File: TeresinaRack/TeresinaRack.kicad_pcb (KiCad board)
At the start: 8 copper layers, 68 x 40 mm, 198 parts, among them J3 USB_Micro-B, J4 SWD, J5 PATCH_SM_EDGE, Q1 MMBT3904, Q2 MMBT3904, SW1 RESET, SW2 BOOT, U1 STM32H750IBK6, U12 TL074, U13 MCP6004, U14 MCP6004, U15 MCP6004, U16 LM4040DBZ-10, U2 IS25LP064A, U3 AS4C16M32MSA-6BIN, U4 PCM3060, U6 TPS62170DSGR, U7 LD1117S50, U8 USBLC6-2SC6, Y1 16MHz

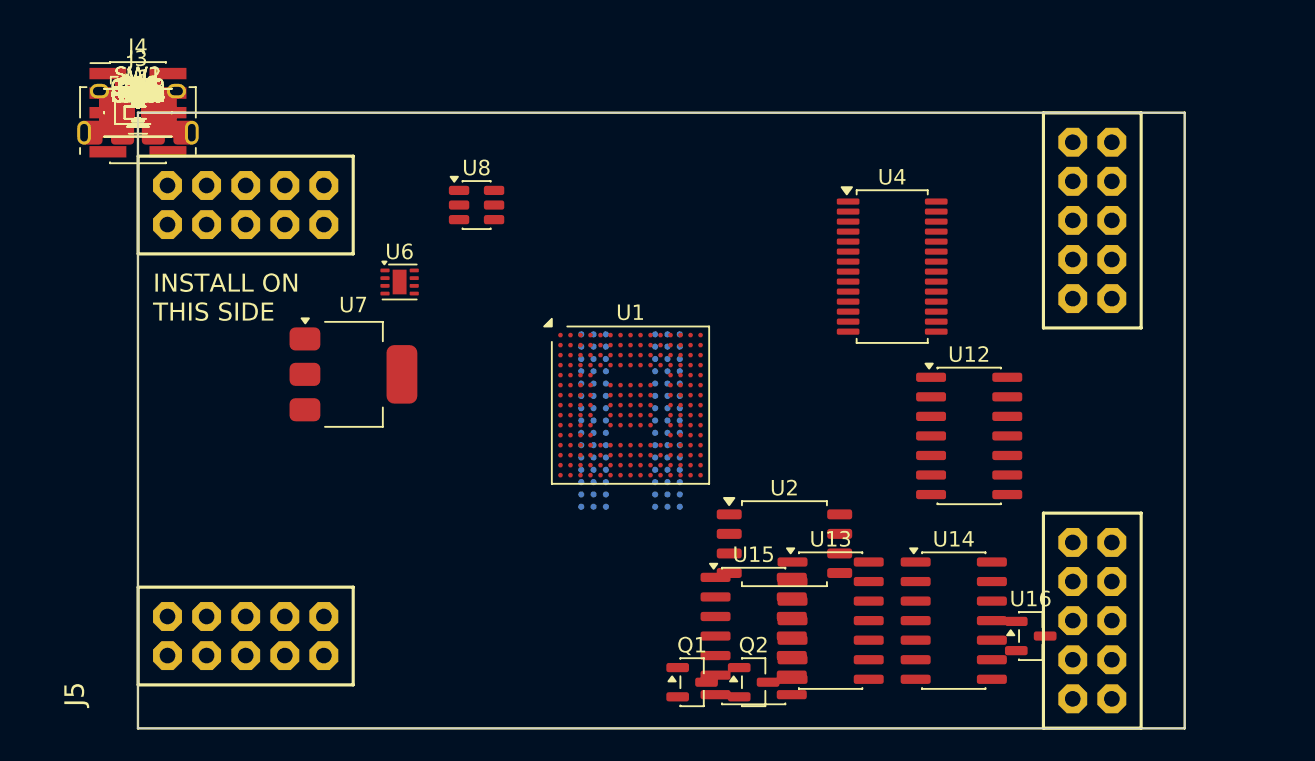
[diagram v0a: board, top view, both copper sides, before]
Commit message: PCB: placement, power/ground planes, BGA via-in-pad fanout
Full double-sided placement on the 68x40 outline (digital core, analog
partition, connector-driven). In1=GND / In6=+3V3 planes plus F/B ground
fills. SDRAM offset from the STM32 so both BGAs use through-via-in-pad;
253 vias bond all power/ground balls to the planes and give signal balls
inner-layer escapes. Signal routing pending.
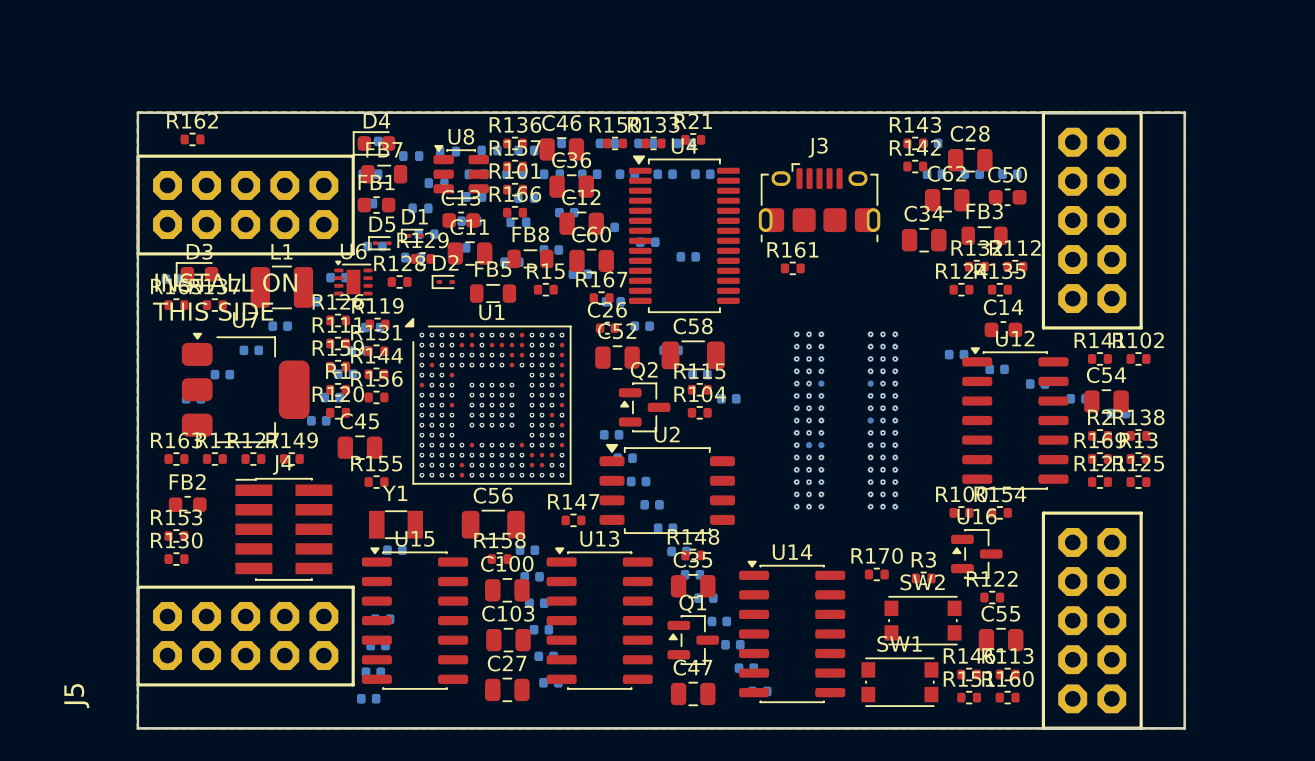
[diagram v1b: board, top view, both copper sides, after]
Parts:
- C1, C10, C101, C102, C104, C105, C112, C113, C120, C121, C122, C123, C124, C125, C126, C127, C128, C129, C130, C131, C132, C133, C134, C135, C136, C137, C138, C139, C140, C141, C142, C143, C15, C16, C17, C18, C19, C2, C20, C21, C22, C23, C24, C25, C29, C3, C30, C31, C32, C37, C38, C39, C4, C44, C48, C5, C51, C53, C57, C59, C6, C61, C63, C7, C8, C9, R103, R105, R110, R114, R116, R117, R118, R12, R123, R134, R139, R14, R140, R145, R152, R164, R168, R4: moved to B.Cu
- moved R125 69.3 mm to (65.0, 24.0)
- moved R13 68.8 mm to (65.0, 22.5)
- moved R138 68.3 mm to (65.0, 21.0)
- moved R160 68.1 mm to (56.5, 38.0)
- moved R113 67.3 mm to (56.5, 36.5)
- moved R121 66.9 mm to (62.5, 24.0)
- moved R102 66.9 mm to (65.0, 16.0)
- moved C3 66.6 mm to (63.7, 19.5), turned to 180 degrees
- moved R169 66.4 mm to (62.5, 22.5)
- moved R151 66.0 mm to (54.0, 38.0)
- moved R2 65.9 mm to (62.5, 21.0)
- moved C55 65.7 mm to (56.1, 34.3)
- moved C54 65.7 mm to (62.9, 18.8)
- moved R146 65.2 mm to (54.0, 36.5)
- moved R141 64.5 mm to (62.5, 16.0)
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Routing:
- net VCAP: vias 0 -> 2
- net USB_DP: vias 0 -> 1
- net USB_DM: vias 0 -> 1
- net SWO: vias 0 -> 1
- net SWDIO: vias 0 -> 1
- net SWCLK: vias 0 -> 1
- net SPI2_SCK: vias 0 -> 1
- net SPI2_CS: vias 0 -> 1
- net SDMMC1_D3: vias 0 -> 1
- net SDMMC1_D2: vias 0 -> 1
- net SDMMC1_D1: vias 0 -> 1
- net SDMMC1_D0: vias 0 -> 1
- net SDMMC1_CMD: vias 0 -> 1
- net SDMMC1_CK: vias 0 -> 1
- net SAI1_SDB: vias 0 -> 1
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- added copper zone on In6.Cu, net +3V3
- added copper zone on B.Cu, net GND
- added copper zone on F.Cu, net GND
- added copper zone on In1.Cu, net GND

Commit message: PCB: route all signal nets (Freerouting)
All signal nets routed on the 8-layer board (FMC, QSPI, SAI, USB, SDMMC,
I2C, audio, CV/gate) with 0 clearance violations; 3675 segments, 664 vias.
Power/ground decoupling-to-plane connections (~106) still to complete.
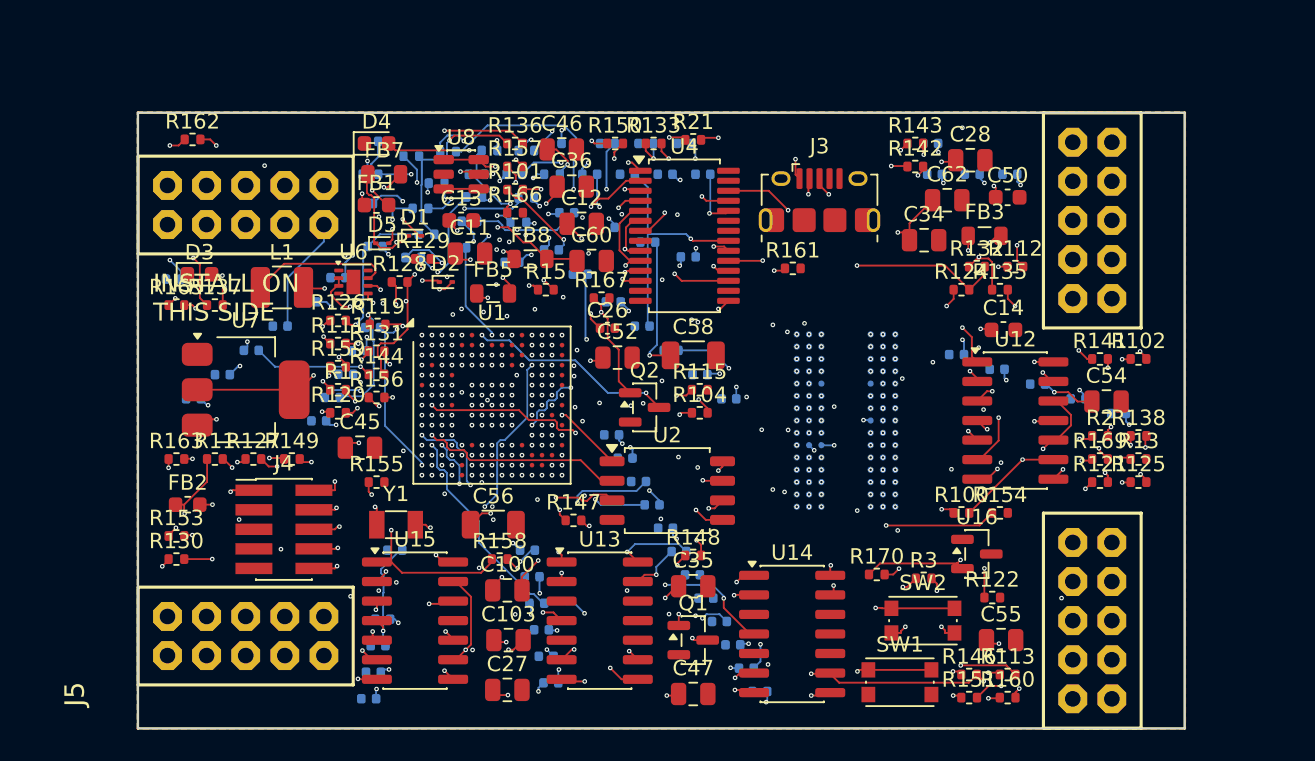
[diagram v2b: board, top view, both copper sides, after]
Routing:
- net VREF_N10: track 0.00 -> 122.1 mm, vias 0 -> 6
- net +3V3A: track 0.00 -> 114.2 mm, vias 2 -> 10
- net -12V: track 0.00 -> 96.2 mm, vias 0 -> 6
- net +12V: track 0.00 -> 95.0 mm, vias 0 -> 7
- net NRST: track 0.00 -> 94.1 mm, vias 1 -> 6
- net +5V: track 0.00 -> 92.7 mm, vias 0 -> 4
- net SUM_3: track 0.00 -> 89.0 mm, vias 0 -> 4
- net SUM_2: track 0.00 -> 85.2 mm, vias 0 -> 5
- net SUM_4: track 0.00 -> 83.6 mm, vias 0 -> 6
- net LINL_M: track 0.00 -> 82.8 mm, vias 0 -> 4
- net N_OLA: track 0.00 -> 82.2 mm, vias 0 -> 5
- net CVO_FILT_2: track 0.00 -> 78.1 mm, vias 0 -> 4
- net CV_3: track 0.00 -> 78.0 mm, vias 1 -> 5
- net SUM_7: track 0.00 -> 77.3 mm, vias 0 -> 5
- net ADC_12: track 0.00 -> 77.0 mm, vias 1 -> 4
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
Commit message: PCB: complete routing, DRC-clean
Stitched every power pad to the GND/+3V3 planes (168 fan-out vias) and routed
all remaining signals (Freerouting 2.x + a custom A* finisher for the last net).
Cleared all clearance, board-edge, thermal-relief and courtyard errors:
0 DRC errors, 0 shorts, all 238 nets connected.
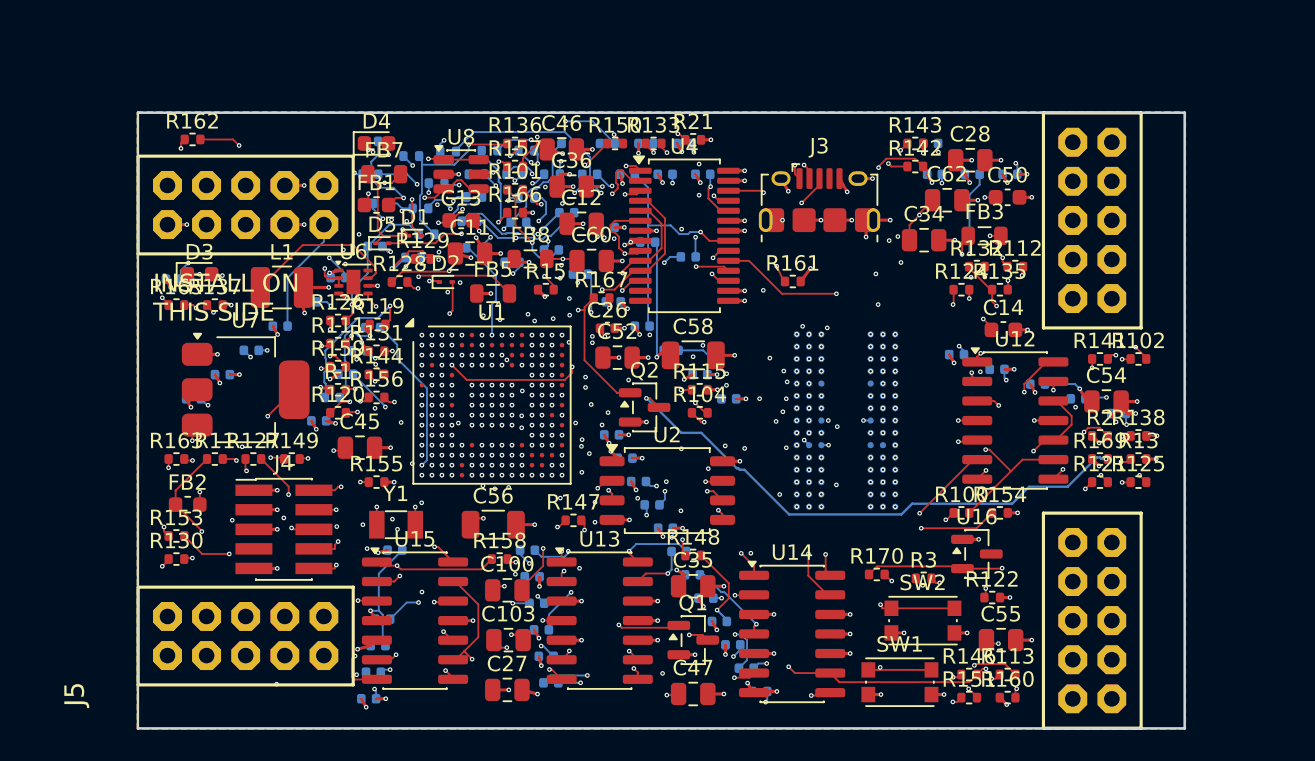
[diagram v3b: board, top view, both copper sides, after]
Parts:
- moved R161 0.85 mm to (42.5, 11.0)
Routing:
- net GND: track 0.00 -> 96.5 mm, vias 53 -> 165
- net +3V3A: track 114.2 -> 137.4 mm, vias 10 -> 9
- net SDMMC1_D0: track 22.4 -> 36.3 mm
- net FMC_SDNWE: track 38.4 -> 24.8 mm, vias 4 -> 2
- net FMC_SDCKE0: track 42.8 -> 32.3 mm
- net ADCJACK_11: track 56.9 -> 46.9 mm, vias 2 -> 1
- net VREF_N10: track 122.1 -> 112.3 mm, vias 6 -> 7
- net FMC_SDNCAS: track 35.4 -> 26.7 mm
- net SUM_3: track 89.0 -> 80.4 mm, vias 4 -> 5
- net SUM_5: track 76.8 -> 68.3 mm
- net CV_4: track 63.1 -> 54.6 mm, vias 4 -> 3
- net A_IN: track 72.0 -> 80.5 mm
- net RINR_M: track 49.3 -> 57.5 mm, vias 2 -> 3
- net SDMMC1_CK: track 27.3 -> 35.4 mm
- net FB_BK: track 64.8 -> 72.7 mm, vias 5 -> 4
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
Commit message: PCB: remove dangling router stubs, tidy silkscreen
Strip the 21 single-ended router stubs left by the autorouter, hide component
values, and set reference designators to the 0.8mm silk minimum. Still 0 DRC
errors, all nets connected.
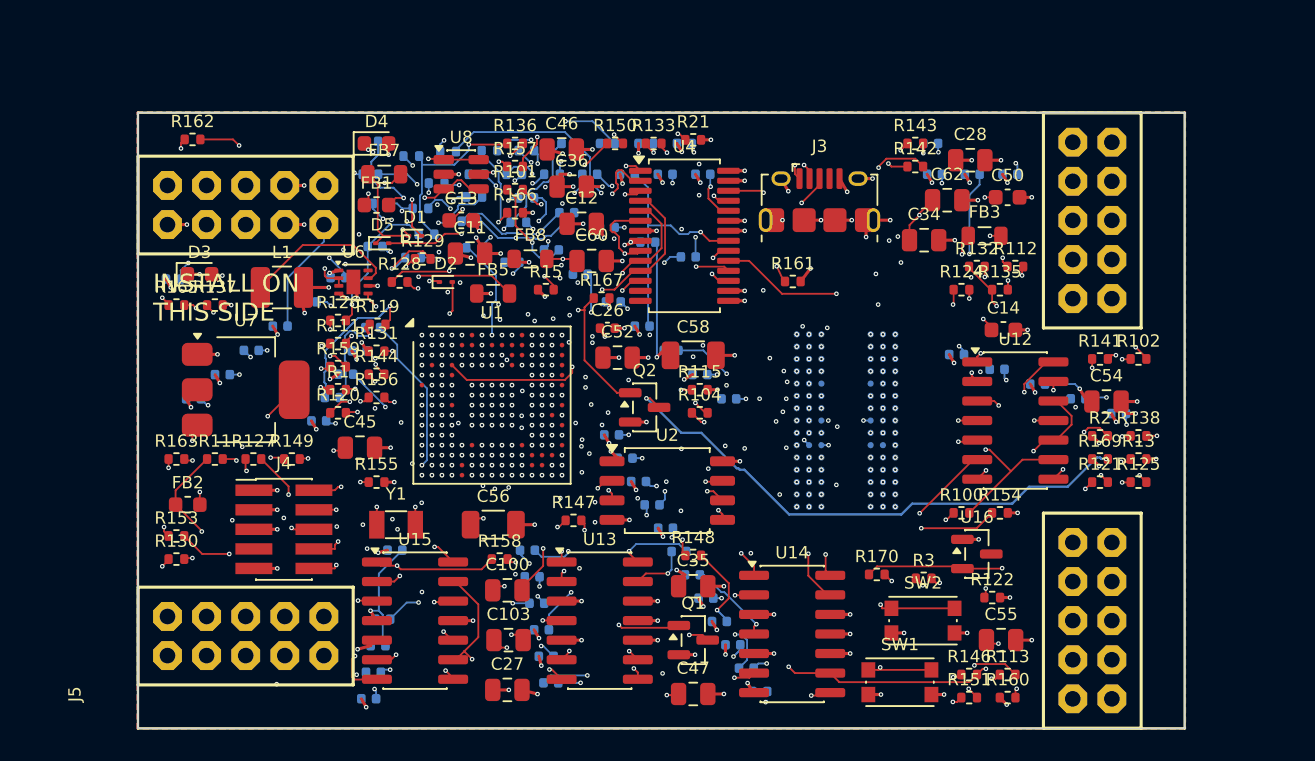
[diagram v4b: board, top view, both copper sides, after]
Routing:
- net +3V3: track 51.7 -> 42.9 mm, vias 85 -> 81
- net CV_6: track 50.3 -> 49.7 mm, vias 5 -> 4
- net FMC_NBL2: vias 4 -> 3

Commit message: PCB: 10-layer re-route with solid GND/+3V3 planes; validation fixes
- 10 layers: In1 solid GND, In6 solid +3V3 (zero traces on either), 8 signal layers
- FMC_A4 routed on In7; GND stitching + USB return vias; fiducials 3xF 1xB
- Schematic: LCSC/MPN part numbers on all parts; removed 13 orphan labels/wires
  (netlist verified identical); ERC/DRC clean; analog paths SPICE-verified
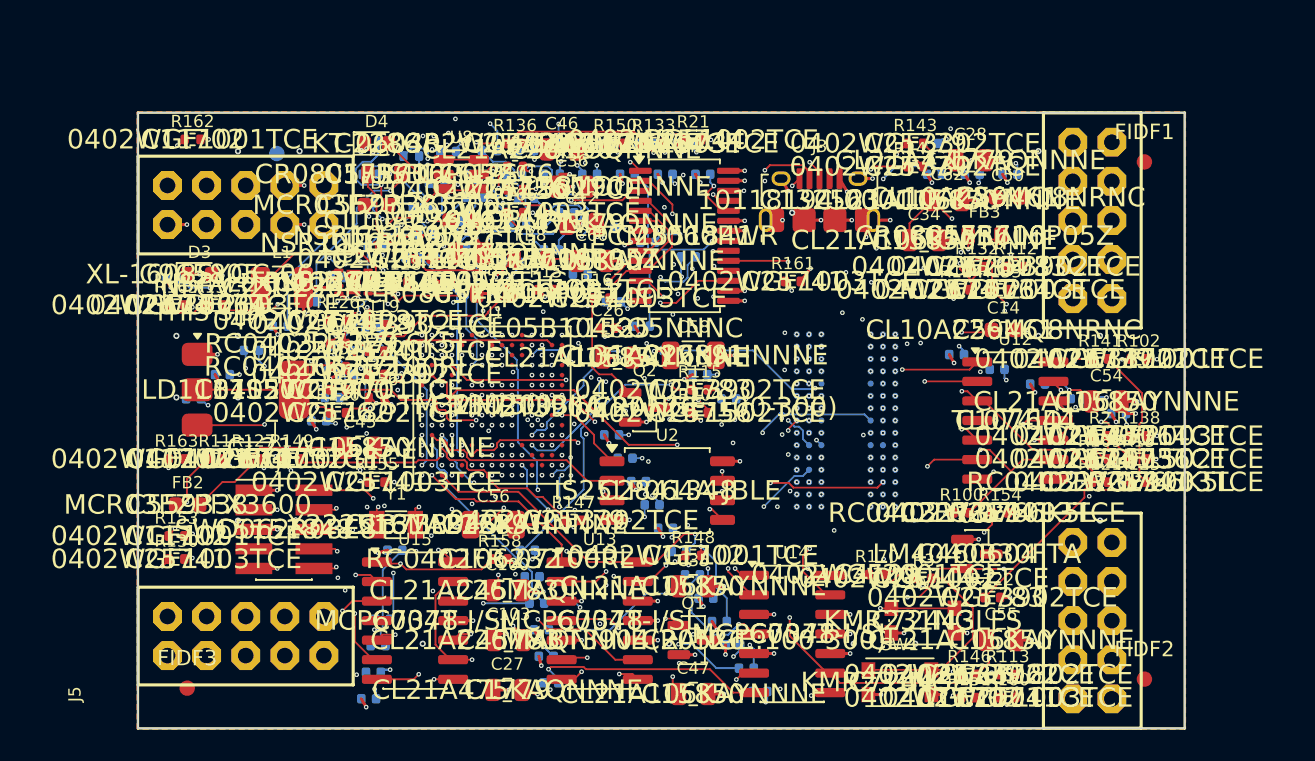
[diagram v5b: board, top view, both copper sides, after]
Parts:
- added FIDB1: Fiducial_1mm_Mask2mm, Fiducial_1mm_Mask2mm, B.Cu at (9.02, 2.65)
- added FIDF1: Fiducial_1mm_Mask2mm, Fiducial_1mm_Mask2mm, F.Cu at (65.4, 3.20)
- added FIDF2: Fiducial_1mm_Mask2mm, Fiducial_1mm_Mask2mm, F.Cu at (65.4, 36.8)
- added FIDF3: Fiducial_1mm_Mask2mm, Fiducial_1mm_Mask2mm, F.Cu at (3.20, 37.4)
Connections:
- U3 pad E3: (no net) -> NC_U3_E3
- U3 pad E7: (no net) -> NC_U3_E7
- U3 pad H7: (no net) -> NC_U3_H7
- U3 pad K2: (no net) -> NC_U3_K2
- U3 pad K3: (no net) -> NC_U3_K3
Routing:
- net USB_DP: track 68.6 -> 93.5 mm, vias 5 -> 6
- net VCAP: track 50.7 -> 65.1 mm
- net SAI1_MCLK: track 20.2 -> 34.4 mm, vias 3 -> 2
- net CV_2: track 62.3 -> 75.2 mm, vias 7 -> 6
- net SDMMC1_D0: track 36.3 -> 23.8 mm, vias 1 -> 2
- net N_ORB: track 69.4 -> 79.6 mm, vias 6 -> 5
- net CVOUT_2: track 66.9 -> 57.1 mm, vias 2 -> 1
- net OSC_OUT: track 54.5 -> 64.2 mm
- net SUM_1: track 61.7 -> 71.3 mm, vias 5 -> 6
- net FMC_A8: track 30.8 -> 40.2 mm, vias 4 -> 2
- net CV_5: track 40.4 -> 49.5 mm
- net SUM_2: track 81.1 -> 89.8 mm, vias 5 -> 4
- net LD_IN: track 25.5 -> 34.2 mm, vias 3 -> 2
- net FMC_A3: track 38.3 -> 29.9 mm, vias 3 -> 2
- net N_LINA: track 35.5 -> 43.4 mm, vias 2 -> 3
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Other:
- copper layers 8 -> 10
